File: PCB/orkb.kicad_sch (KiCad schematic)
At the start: 82 parts, among them J1 USB_C_Receptacle_USB2.0, P1 OLED, SW1 MXHS, SW10 MXHS, SW11 MXHS, SW12 MXHS, SW13 MXHS, SW14 MXHS, SW15 MXHS, SW16 MXHS, SW17 MXHS, SW18 MXHS, SW19 MXHS, SW2 MXHS, SW20 MXHS, SW21 MXHS, SW22 MXHS, SW23 MXHS, SW3 MXHS, SW4 MXHS, SW5 MXHS, SW6 MXHS, SW7 MXHS, SW8 MXHS, SW9 MXHS, U1 ProMicro, U2 SRV05-4, U3 SRV05-4

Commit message: Added support for LED in schematic
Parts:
- added JP3, JP4: Jumper_2_Open, SplitKeyboard_Common:Jumper_min_v2, symbol Jumper:Jumper_2_Open
- added LED1, LED10, LED11, LED12, LED13, LED14, LED15, LED16, LED17, LED18, LED19, LED2, LED20, LED21, LED22, LED23, LED3, LED4, LED5, LED6, LED7, LED8, LED9: SK6803MINI-E, SplitKeyboard_Common:MX_SK6812MINI-E_REVERSIBLE, symbol SplitKeyboard_Common:SK6812MINI-E
- added SW24, SW25: MSK12C02, SplitKeyboard_Common:MSK12C02, symbol SplitKeyboard_Common:MSK12C02
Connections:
- net GND: now also LED1.3 (GND), LED10.3 (GND), LED11.3 (GND), LED12.3 (GND), LED13.3 (GND), LED14.3 (GND), LED15.3 (GND), LED16.3 (GND), LED17.3 (GND), LED18.3 (GND), LED19.3 (GND), LED2.3 (GND), LED20.3 (GND), LED21.3 (GND), LED22.3 (GND), LED23.3 (GND), LED3.3 (GND), LED4.3 (GND), LED5.3 (GND), LED6.3 (GND), LED7.3 (GND), LED8.3 (GND), LED9.3 (GND), SW24.MP (GND), SW25.MP (GND)
- net VCC: now also JP3.1 (A), JP4.1 (A), SW24.COM, SW25.COM
- net LED: now reaches U1.1 (TX0/PD3)
- net LED: now also LED1.4 (DIN)
- new net: LED19.4 (DIN), LED20.2 (DOUT)
- new net: LED4.2 (DOUT), LED5.4 (DIN)
- new net: LED3.2 (DOUT), LED4.4 (DIN)
- new net: LED10.4 (DIN), LED11.2 (DOUT)
- new net: LED11.4 (DIN), LED12.2 (DOUT)
- new net: LED14.2 (DOUT), LED15.4 (DIN)
- new net: LED13.2 (DOUT), LED14.4 (DIN)
- new net: LED20.4 (DIN), LED21.2 (DOUT)
- new net: LED13.4 (DIN), LED7.2 (DOUT)
- new net: LED7.4 (DIN), LED8.2 (DOUT)
- new net: LED1.2 (DOUT), LED2.4 (DIN)
- new net: LED2.2 (DOUT), LED3.4 (DIN)
- new net: LED21.4 (DIN), LED22.2 (DOUT)
- new net: LED22.4 (DIN), LED23.2 (DOUT)
- new net: LED15.2 (DOUT), LED16.4 (DIN)
- new net: LED12.4 (DIN), LED6.2 (DOUT)
- new net: LED5.2 (DOUT), LED6.4 (DIN)
- new net: LED8.4 (DIN), LED9.2 (DOUT)
- new net: LED16.2 (DOUT), LED17.4 (DIN)
- new net: LED10.2 (DOUT), LED9.4 (DIN)
- new net: LED17.2 (DOUT), LED18.4 (DIN)
- new net: LED18.2 (DOUT), LED23.4 (DIN)
- new net PWR_GLOW: JP3.2 (B), SW24.NC, SW25.NC
- new net PWR_KEY: JP4.2 (B), LED1.1 (VDD), LED10.1 (VDD), LED11.1 (VDD), LED12.1 (VDD), LED13.1 (VDD), LED14.1 (VDD), LED15.1 (VDD), LED16.1 (VDD), LED17.1 (VDD), LED18.1 (VDD), LED19.1 (VDD), LED2.1 (VDD), LED20.1 (VDD), LED21.1 (VDD), LED22.1 (VDD), LED23.1 (VDD), LED3.1 (VDD), LED4.1 (VDD), LED5.1 (VDD), LED6.1 (VDD), LED7.1 (VDD), LED8.1 (VDD), LED9.1 (VDD), SW24.NO, SW25.NO
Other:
- note added: "ToDo: Implement underglow"
- note removed: "ToBe: used for LED"
- moved on the sheet: JP1, JP2, RES1, RES2

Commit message: Updated PCB with LED and switch
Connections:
- net PWR_GLOW: now also JP3.1 (A); no longer JP3.2 (B)
- net PWR_KEY: now also JP4.1 (A); no longer JP4.2 (B)
- net VCC: now also JP3.2 (B), JP4.2 (B); no longer JP3.1 (A), JP4.1 (A)
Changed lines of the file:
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@@
 		(lib_id "Jumper:Jumper_2_Open")
 		(at 358.14 55.88 0)
+		(mirror y)
 		(unit 1)
 		(exclude_from_sim yes)
@@
 		(lib_id "Jumper:Jumper_2_Open")
 		(at 358.14 49.53 0)
+		(mirror y)
 		(unit 1)
 		(exclude_from_sim yes)

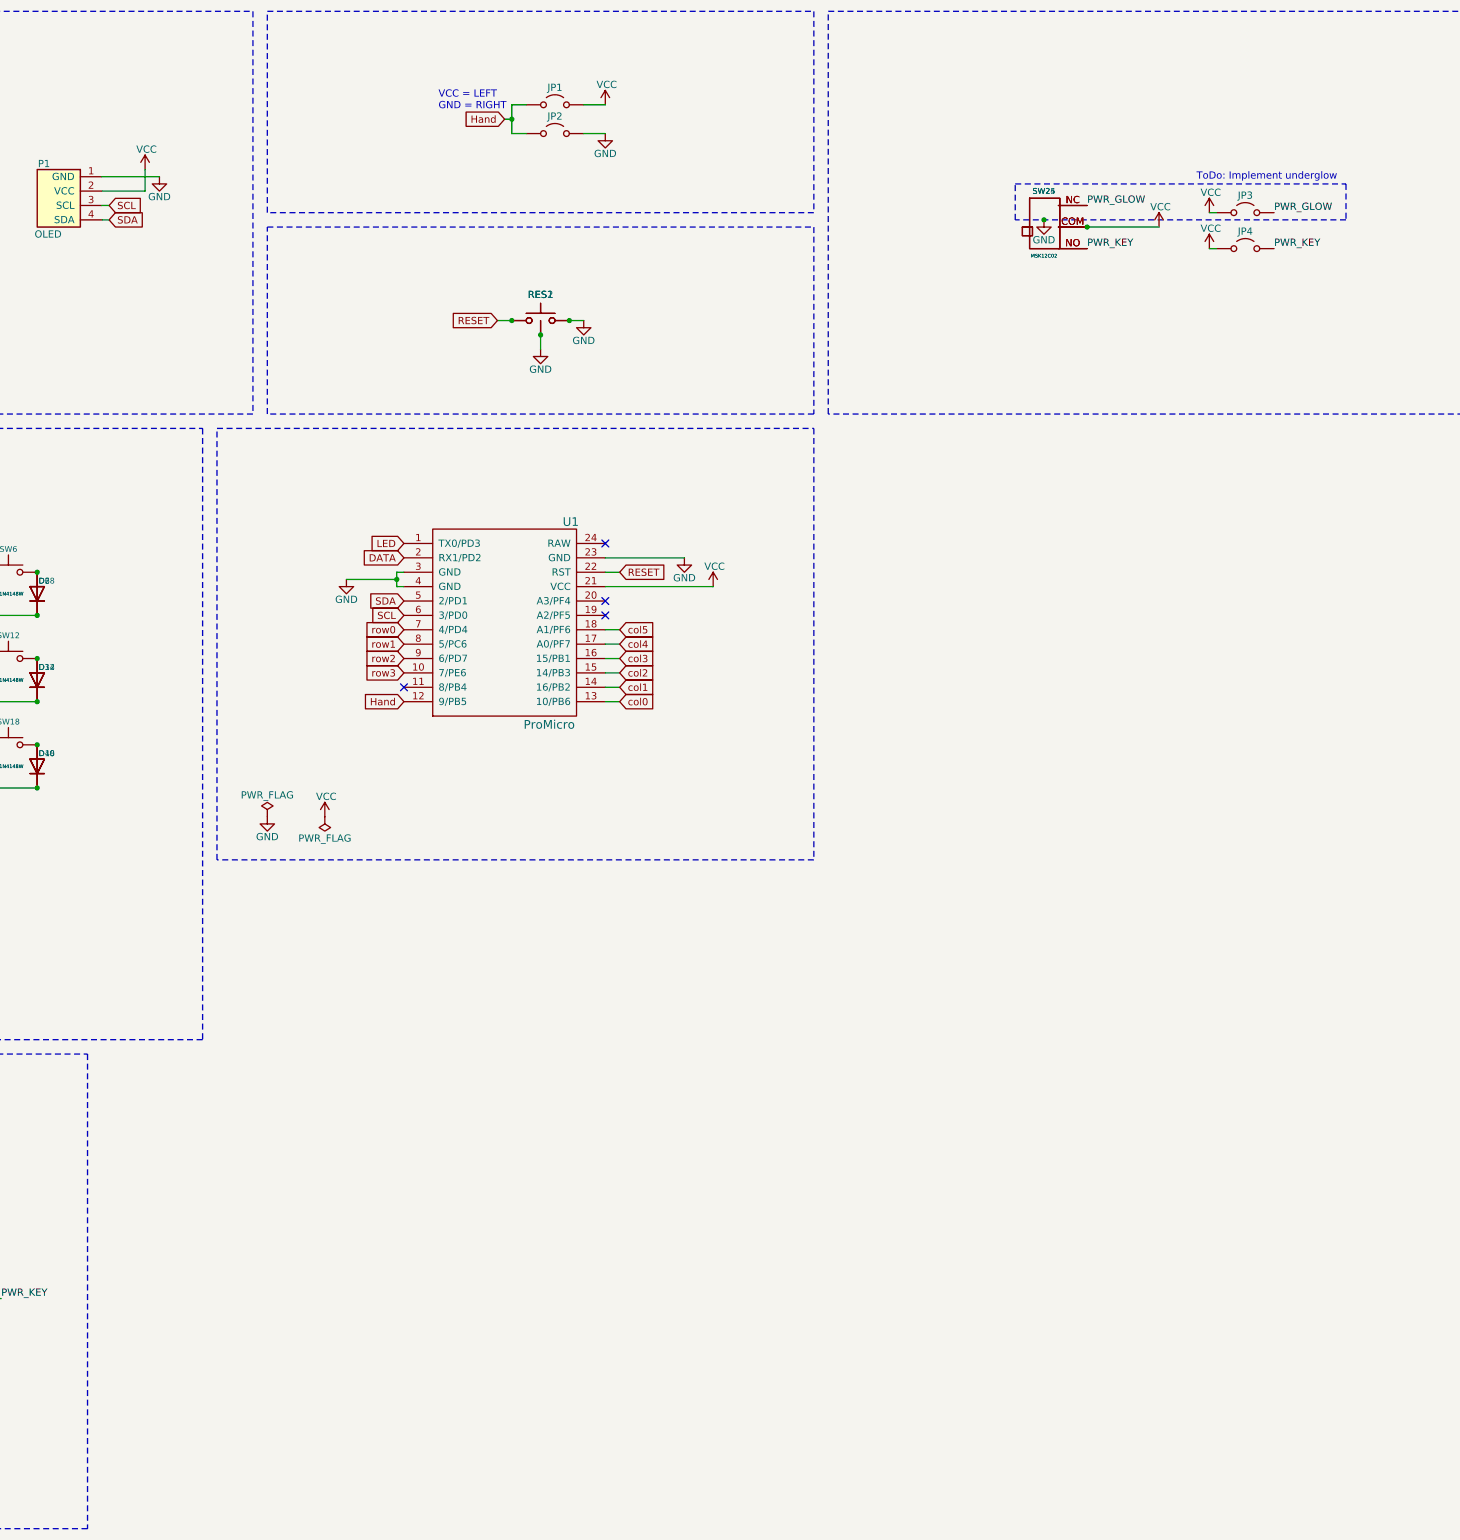
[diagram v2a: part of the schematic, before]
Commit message: Added underglow LED to schematic
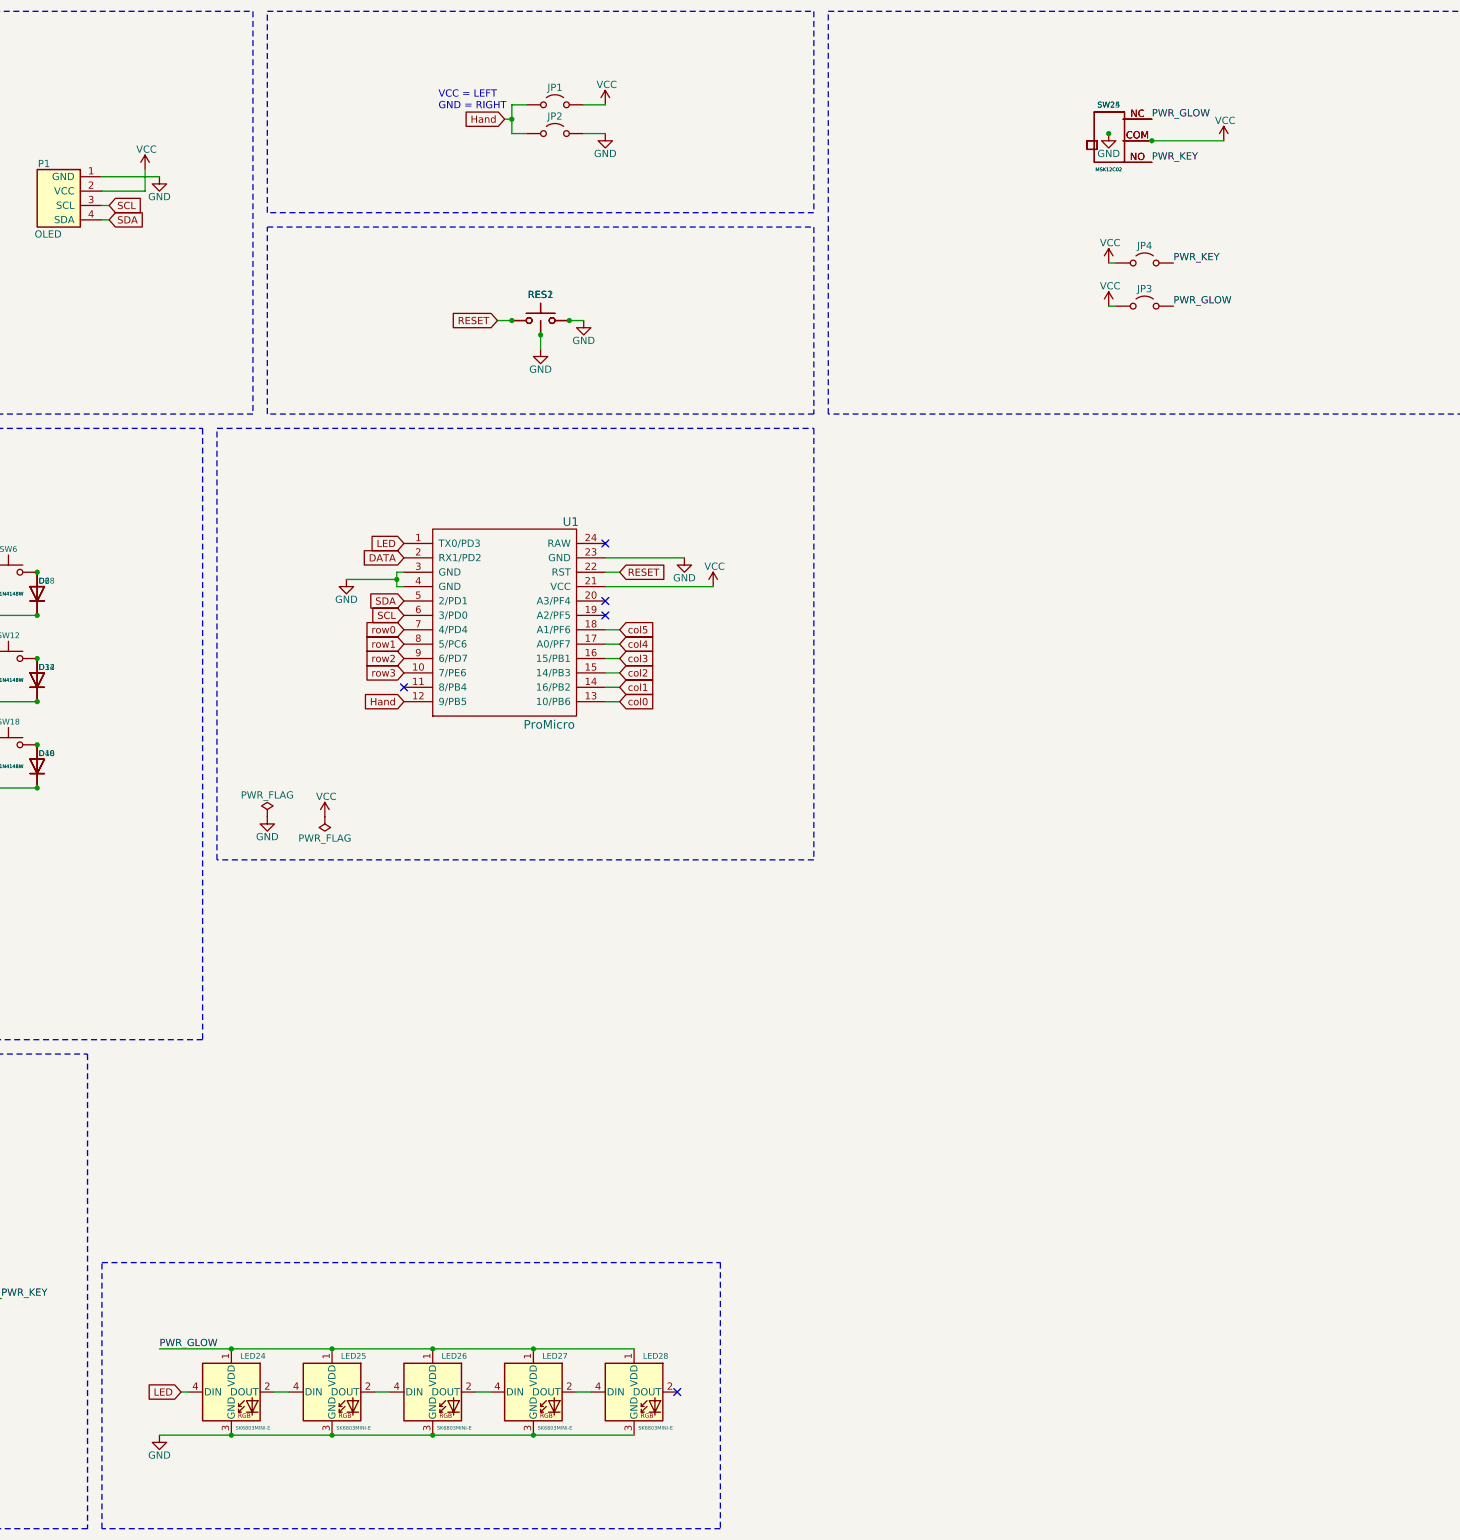
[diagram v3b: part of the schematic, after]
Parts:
- added LED24, LED25, LED26, LED27, LED28: SK6803MINI-E, SplitKeyboard_Common:MX_SK6812MINI-E_REVERSIBLE, symbol SplitKeyboard_Common:SK6812MINI-E
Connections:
- net GND: now also LED24.3 (GND), LED25.3 (GND), LED26.3 (GND), LED27.3 (GND), LED28.3 (GND)
- net LED: now also LED24.4 (DIN)
- net PWR_GLOW: now also LED24.1 (VDD), LED25.1 (VDD), LED26.1 (VDD), LED27.1 (VDD), LED28.1 (VDD)
- new net: LED25.2 (DOUT), LED26.4 (DIN)
- new net: LED24.2 (DOUT), LED25.4 (DIN)
- new net: LED26.2 (DOUT), LED27.4 (DIN)
- new net: LED27.2 (DOUT), LED28.4 (DIN)
- no-connect marks 13 -> 14
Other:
- note removed: "ToDo: Implement underglow"
- moved on the sheet: JP3, JP4, SW24, SW25

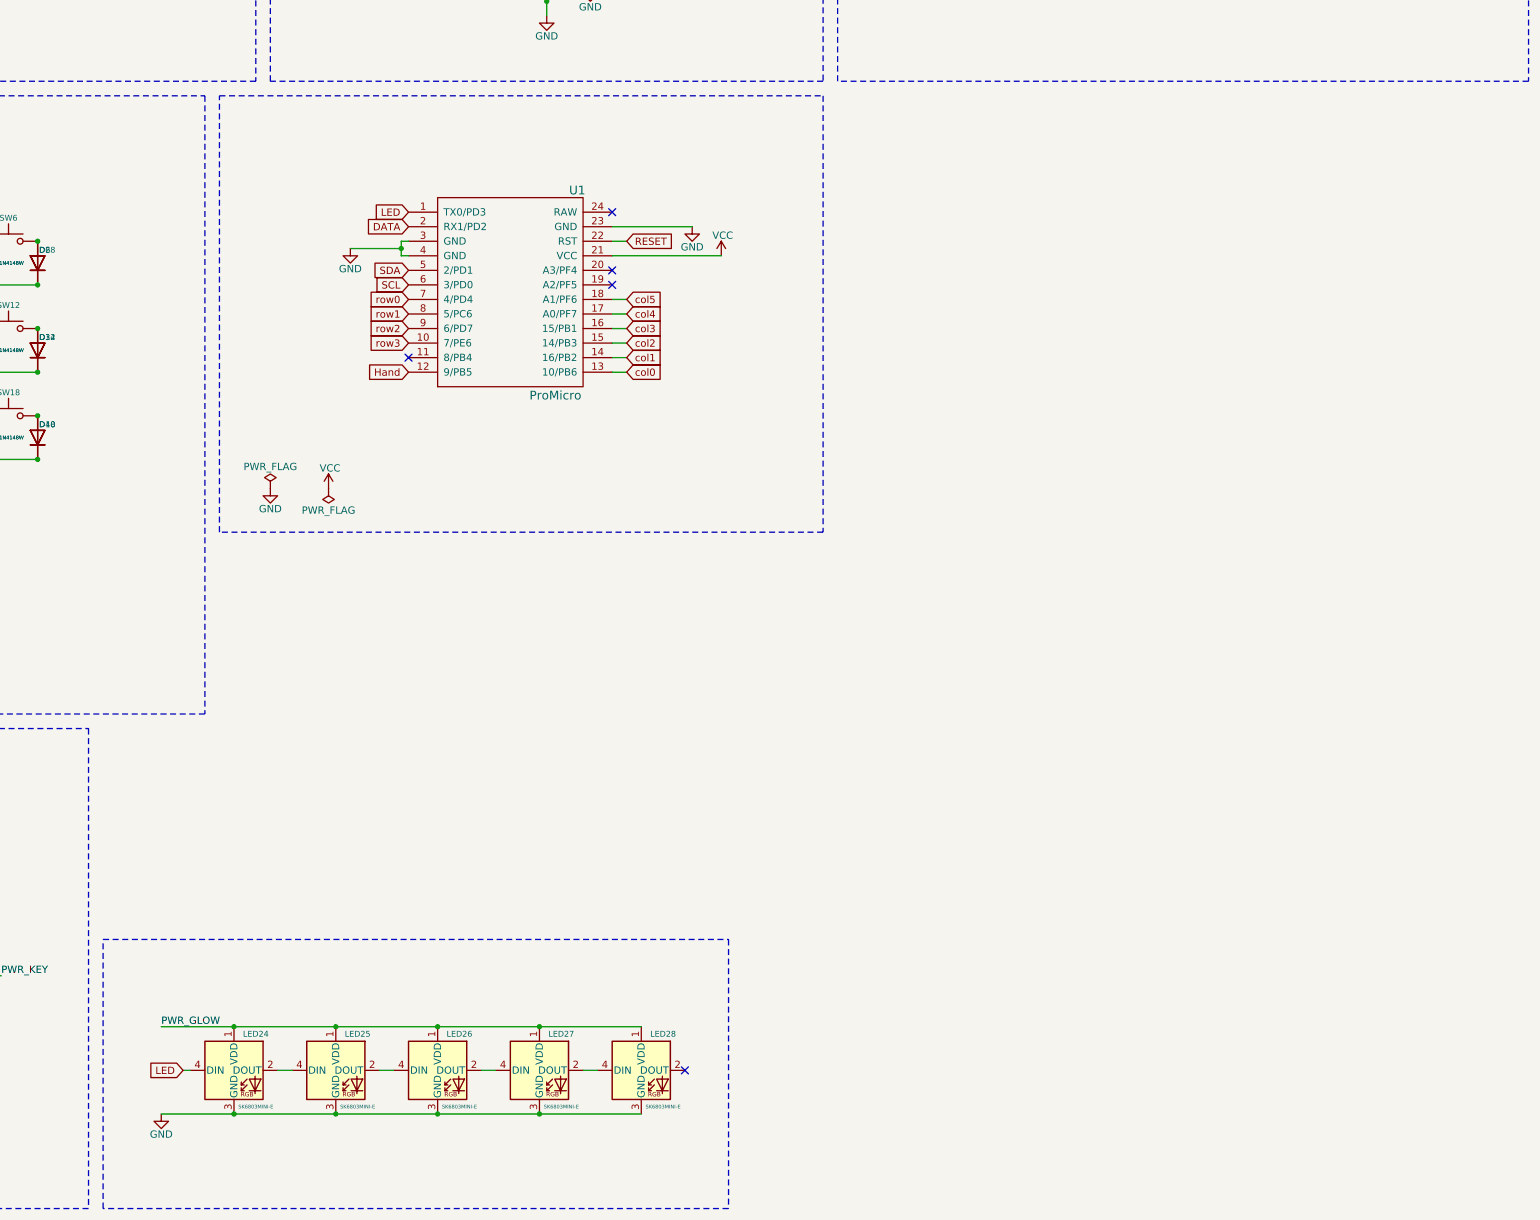
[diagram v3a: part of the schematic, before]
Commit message: Added underglow LEDs to PCB
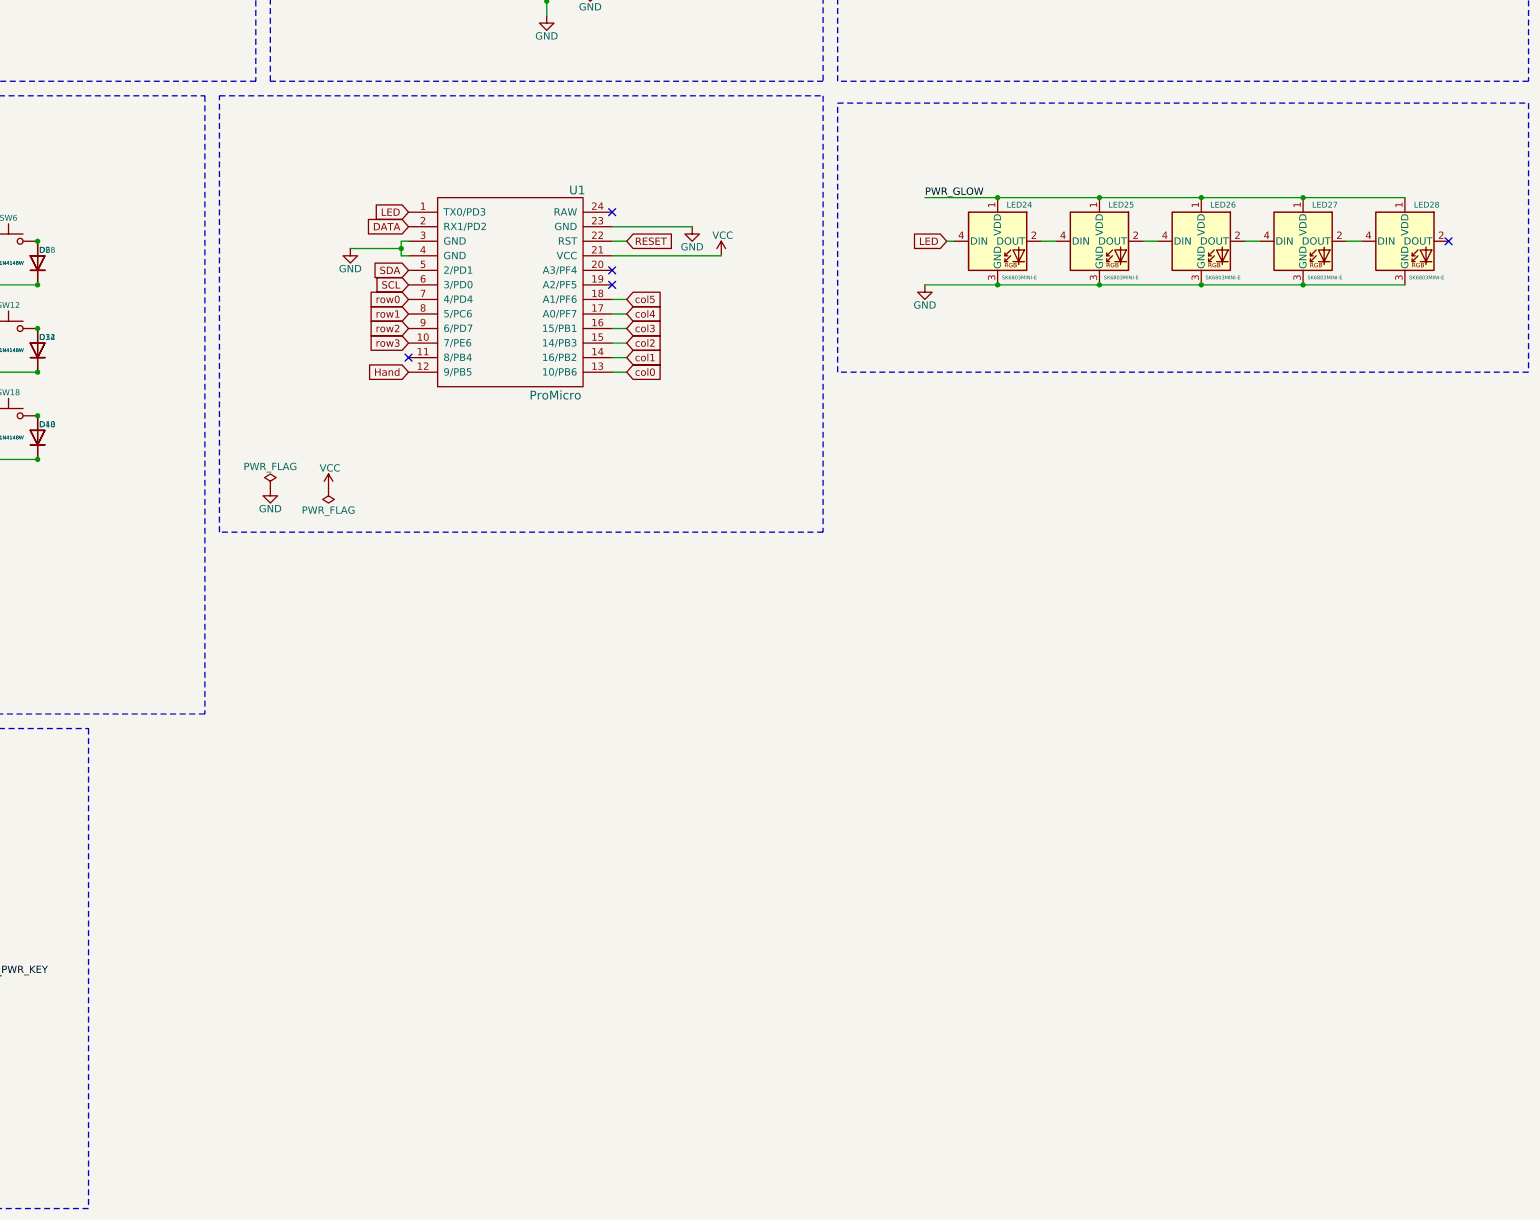
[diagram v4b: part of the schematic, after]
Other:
- moved on the sheet: LED24, LED25, LED26, LED27, LED28
